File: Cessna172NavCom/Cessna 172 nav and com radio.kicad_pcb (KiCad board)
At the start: 2 copper layers, 180 x 38 mm, 52 parts, among them J1 Conn_02x12_Odd_Even, J2 Barrel_Jack_MountingPin, J3 Conn_01x05, SW1 SW_Push, SW2 SW_Push, SW3 SW_Push, SW4 Tuning encoder, SW5 Tuning encoder, SW6 Tuning encoder, U1 MAX7219 COM standby, U2 3651A, U3 MAX7219 COM standby, U4 3651A, U5 MAX7219 COM standby, U6 3651A, U7 MAX7219 COM standby, U8 3651A

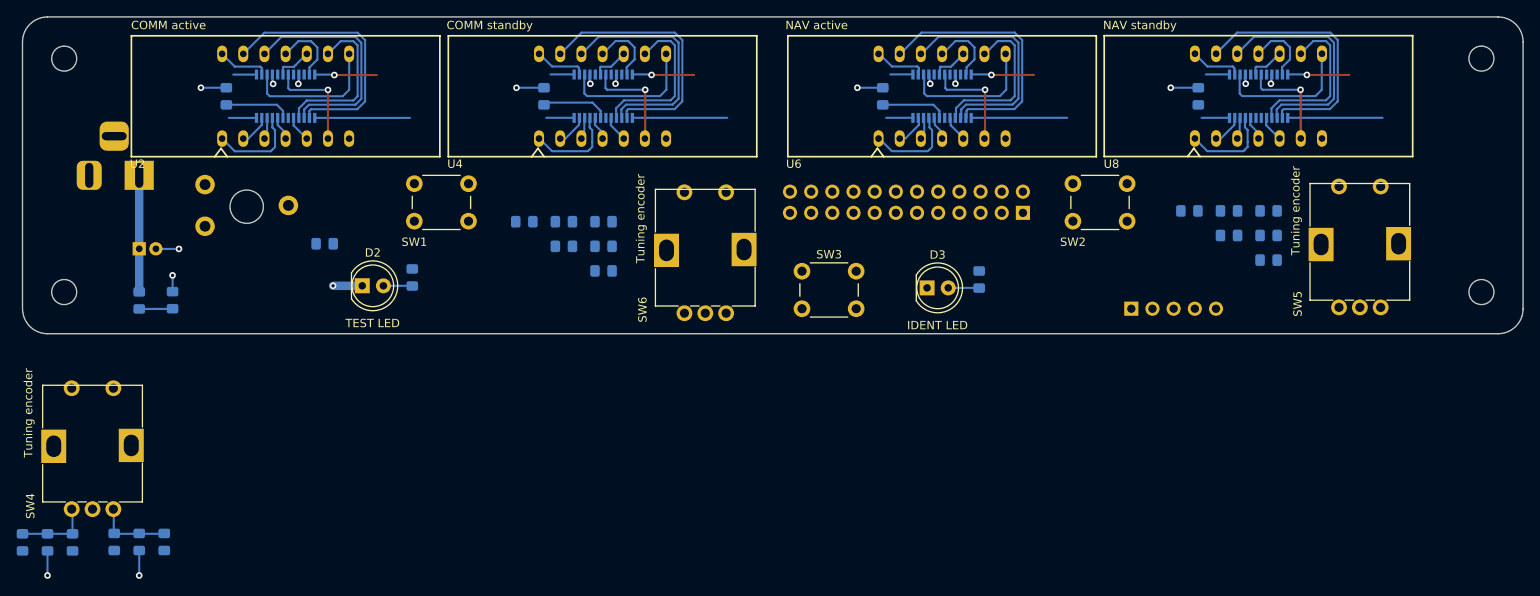
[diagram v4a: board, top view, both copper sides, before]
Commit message: Switch to USB for power, all parts on board
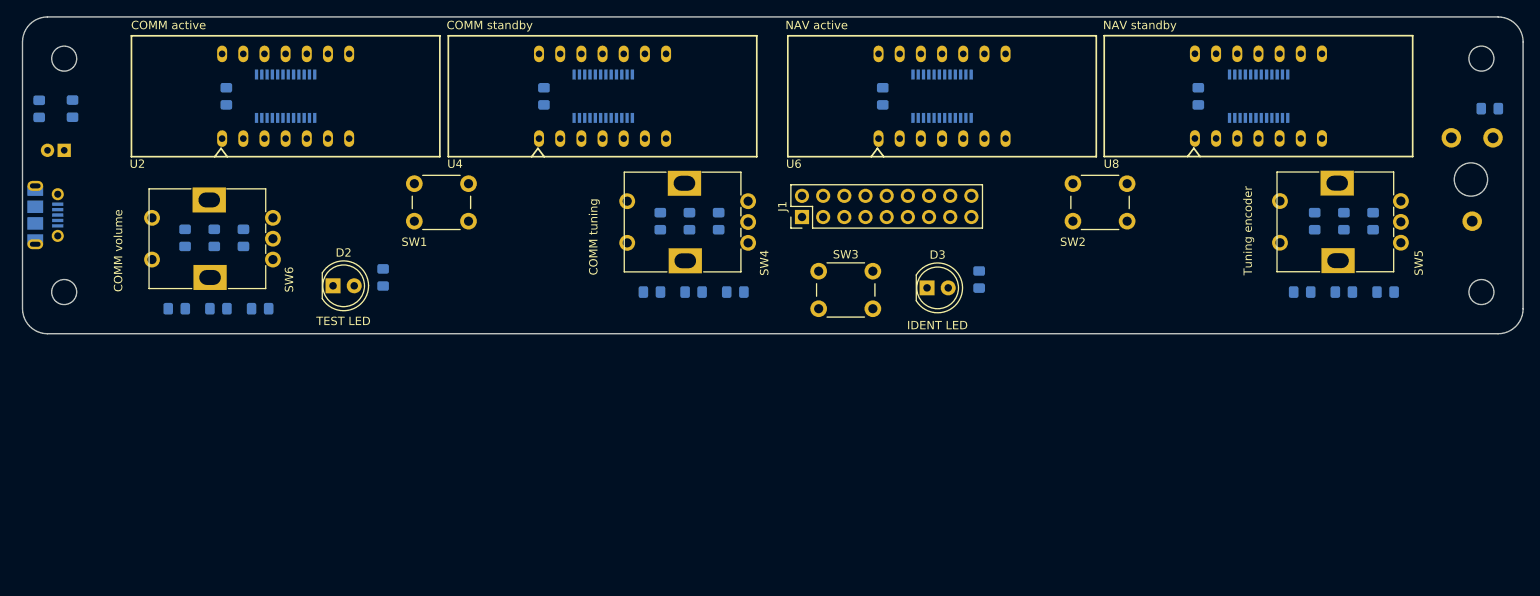
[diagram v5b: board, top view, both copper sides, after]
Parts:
- removed J3: Conn_01x05, Connector_PinHeader_2.54mm:PinHeader_1x05_P2.54mm_Vertical
- J1: value Conn_02x12_Odd_Even -> Conn_02x09_Odd_Even; footprint Connector_PinHeader_2.54mm:PinHeader_2x12_P2.54mm_Vertical -> Connector_PinHeader_2.54mm:PinHeader_2x09_P2.54mm_Vertical; moved to F.Cu
- J2: value Barrel_Jack_MountingPin -> USB_B_Micro; footprint Cessna 172 nav and com radio:BarrelJack_Horizontal -> Connector_USB:USB_Micro-B_Molex-105017-0001
- SW4: value Tuning encoder -> COMM tuning
- SW6: value Tuning encoder -> COMM volume
- moved RV1 154.6 mm to (206.4, 134.5), turned to 270 degrees
- moved R1 140.7 mm to (206.0, 131.0)
- moved R7 85.0 mm to (115.5, 153.0), turned to 180 degrees
- moved C6 83.1 mm to (110.5, 153.0), turned to 180 degrees
- moved R8 82.1 mm to (113.5, 144.5)
- moved R5 81.3 mm to (105.5, 153.0), turned to 0 degrees
- moved C7 76.4 mm to (110.0, 144.5)
- moved SW4 76.0 mm to (109.5, 144.5), turned to 90 degrees
- moved R6 70.9 mm to (106.5, 144.5)
- moved SW6 59.5 mm to (52.5, 146.5), turned to 90 degrees
- moved R14 50.2 mm to (49.5, 146.5), turned to 270 degrees
- moved C10 46.8 mm to (53.5, 155.0)
- moved R13 43.0 mm to (48.5, 155.0), turned to 0 degrees
- moved C11 42.0 mm to (53.0, 146.5), turned to 270 degrees
- moved R15 41.4 mm to (58.5, 155.0)
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- renumbered REF** to H1, REF** to H2, REF** to H3, REF** to H4
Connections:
- J1 pad 1: +5V -> GND
- J1 pad 11: NAV_TX_SW -> COMM_VOL_LEFT
- J1 pad 13: COMM_VOL_LEFT -> COMM_VOL_RIGHT
- J1 pad 15: COMM_VOL_RIGHT -> IDENT_SW
- J1 pad 17: IDENT_SW -> IDENT_LED
- J1 pad 3: GND -> NAV_LEFT
- J1 pad 5: NAV_LEFT -> NAV_RIGHT
- J1 pad 7: NAV_RIGHT -> NAV_KHZ_SW
- J1 pad 9: NAV_KHZ_SW -> NAV_TX_SW
- J2 pad 2: GND -> Net-(J2-Pad2)
- U7 pad 24: DOUT -> /sheet5F613961/DOUT
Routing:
- net CLK: track 45.7 -> 0.00 mm
- net +5V: track 37.4 -> 0.00 mm
- net GND: track 36.1 -> 0.00 mm, vias 17 -> 0
- net /sheet5F613961/SEG_A: track 31.4 -> 0.00 mm
- net /sheet5F611637/SEG_A: track 31.4 -> 0.00 mm
- net /5 digit LCD display/SEG_A: track 31.4 -> 0.00 mm
- net /sheet5F613960/SEG_A: track 31.4 -> 0.00 mm
- net LOAD: track 29.8 -> 0.00 mm, vias 4 -> 0
- net /sheet5F613961/SEG_F: track 27.9 -> 0.00 mm
- net /sheet5F613960/SEG_F: track 27.9 -> 0.00 mm
- net /sheet5F611637/SEG_F: track 27.9 -> 0.00 mm
- net /5 digit LCD display/SEG_F: track 27.9 -> 0.00 mm
- net /sheet5F613961/SEG_B: track 19.3 -> 0.00 mm
- net /sheet5F613960/SEG_B: track 19.3 -> 0.00 mm
- net /sheet5F611637/SEG_B: track 19.3 -> 0.00 mm
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
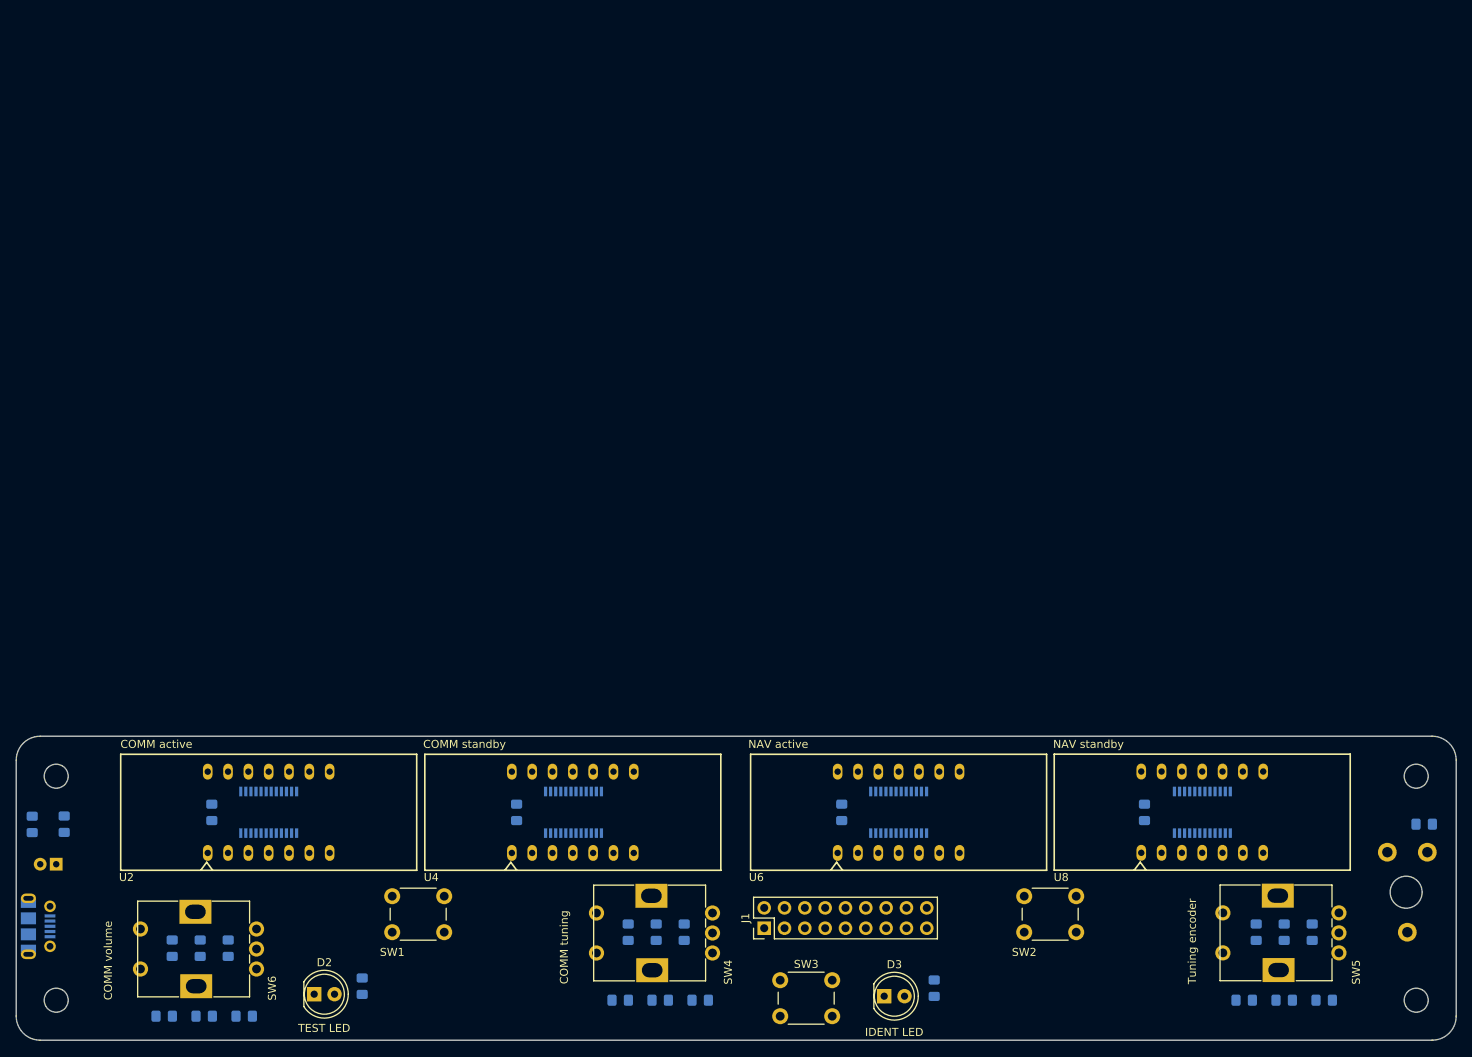
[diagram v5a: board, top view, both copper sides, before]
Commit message: Updated board size and parts placement
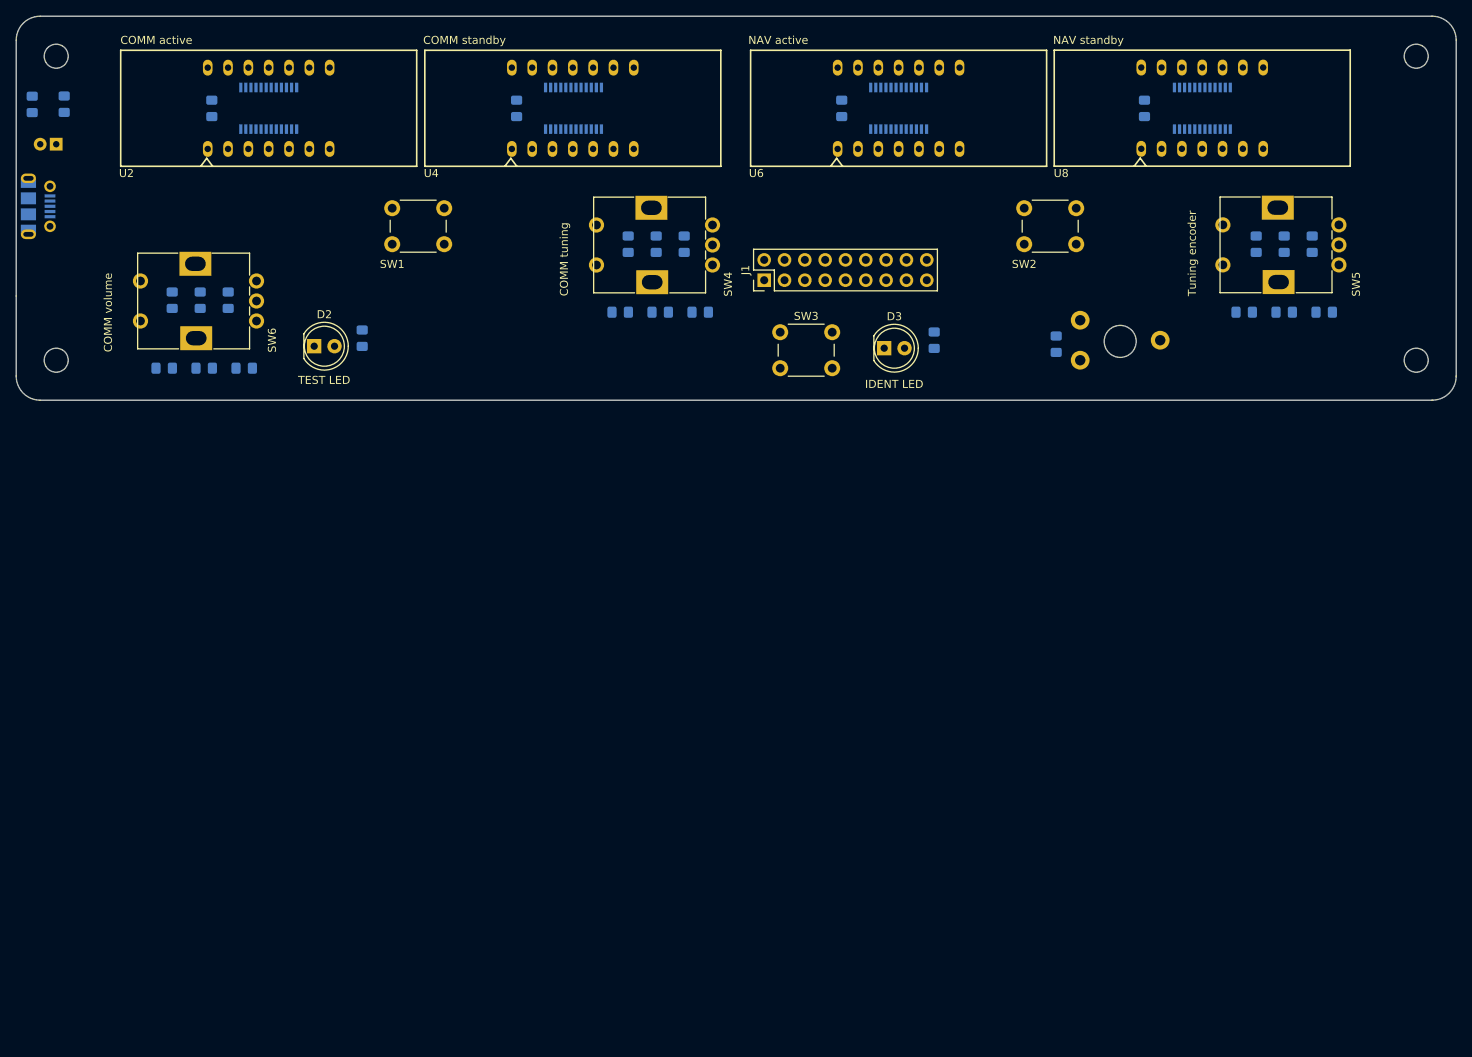
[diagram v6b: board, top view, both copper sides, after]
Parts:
- moved C1 90.0 mm to (35.0, 46.0)
- moved D1 90.0 mm to (32.0, 41.0)
- moved H1 90.0 mm to (35.0, 35.0)
- moved H3 90.0 mm to (205.0, 35.0)
- moved J2 90.0 mm to (32.8, 53.8)
- moved R2 90.0 mm to (36.0, 41.0)
- moved U1 88.0 mm to (61.6, 41.5)
- moved U2 88.0 mm to (61.6, 41.5)
- moved U3 88.0 mm to (99.7, 41.5)
- moved U4 88.0 mm to (99.6, 41.5)
- moved U5 88.0 mm to (140.3, 41.5)
- moved U6 88.0 mm to (140.3, 41.5)
- moved U7 88.0 mm to (178.3, 41.5)
- moved U8 88.0 mm to (178.3, 41.5)
- moved C2 88.0 mm to (54.5, 41.5)
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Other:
- board size 180 x 38 mm -> 180 x 48 mm

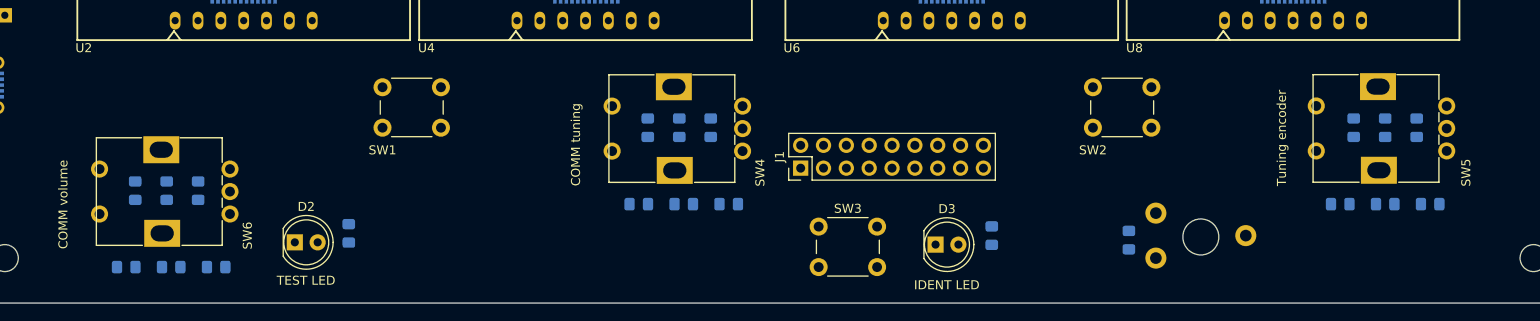
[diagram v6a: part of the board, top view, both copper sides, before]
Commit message: Updated rotary encoder with proper footprint
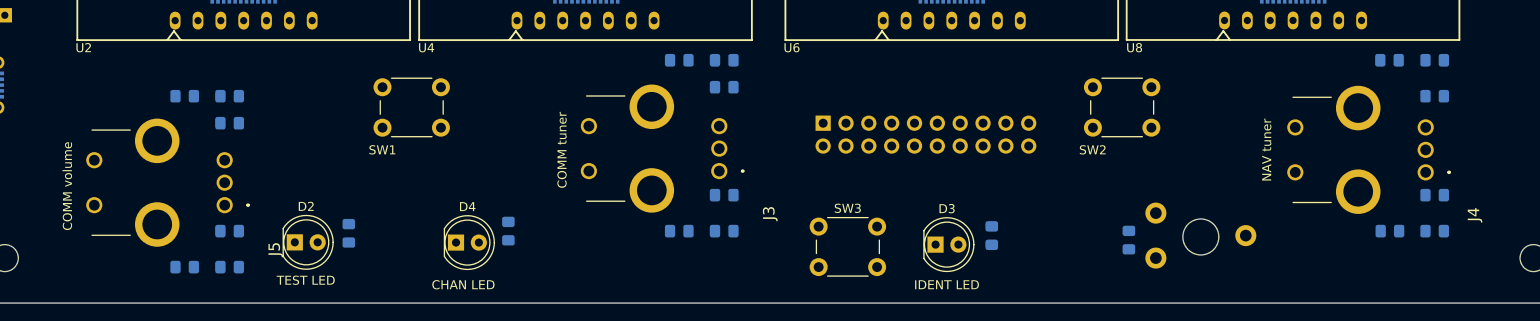
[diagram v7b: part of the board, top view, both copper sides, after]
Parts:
- removed SW4: COMM tuning, Cessna 172 nav and com radio:EN11-HSM1BF20
- removed SW5: Tuning encoder, Cessna 172 nav and com radio:EN11-HSM1BF20
- removed SW6: COMM volume, Cessna 172 nav and com radio:EN11-HSM1BF20
- added D4: LED, LED_THT:LED_D5.0mm, F.Cu at (85.2, 71.3)
- added J3: EN11-HSM1BF20, SamacSys_Parts:EN11HSM1BF20, F.Cu at (114.5, 63.3)
- added J4: EN11-HSM1BF20, SamacSys_Parts:EN11HSM1BF20, F.Cu at (193.0, 63.5)
- added J5: EN11-HSM1BF20, SamacSys_Parts:EN11HSM1BF20, F.Cu at (59.5, 67.1)
- added R17: 220k, Resistor_SMD:R_0805_2012Metric_Pad1.15x1.40mm_HandSolder, B.Cu at (91.0, 70.0)
- J1: value Conn_02x09_Odd_Even -> Conn_02x10_Odd_Even; footprint Connector_PinHeader_2.54mm:PinHeader_2x09_P2.54mm_Vertical -> Connector_PinHeader_2.54mm:PinHeader_2x10_P2.54mm_Vertical; moved to B.Cu
- moved C11 12.6 mm to (60.0, 55.0), turned to 0 degrees
- moved R14 11.9 mm to (55.0, 55.0), turned to 180 degrees
- moved C9 9.30 mm to (194.0, 51.0), turned to 0 degrees
- moved C7 9.01 mm to (115.0, 51.0), turned to 0 degrees
- moved R10 8.49 mm to (189.0, 51.0), turned to 0 degrees
- moved R16 8.28 mm to (60.0, 58.0), turned to 0 degrees
- moved R6 8.28 mm to (110.0, 51.0), turned to 0 degrees
- moved C10 6.50 mm to (60.0, 74.0)
- moved R13 6.50 mm to (55.0, 74.0)
- moved R9 6.29 mm to (189.0, 70.0)
- moved C8 6.26 mm to (194.0, 70.0)
- moved J1 5.59 mm to (126.0, 58.0), turned to 270 degrees
- moved C6 5.41 mm to (115.0, 70.0)
- moved R5 5.41 mm to (110.0, 70.0)
- moved R8 4.74 mm to (115.0, 54.0), turned to 0 degrees
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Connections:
- net /Tuning rotary encoder and switch/A renamed /Tuning rotary encoder and switch/A1
- net /Tuning rotary encoder and switch/B renamed /Tuning rotary encoder and switch/B1
- net /sheet5F5DD32A/A renamed /sheet5F5DD32A/A1
- net /sheet5F5DD32A/B renamed /sheet5F5DD32A/B1
- net /sheet5F5E0D6C/A renamed /sheet5F5E0D6C/A1
- net /sheet5F5E0D6C/B renamed /sheet5F5E0D6C/B1
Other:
- board text added: "CHAN LED"
- board text added: "COMM tuner"
- board text added: "COMM volume"
- board text added: "NAV tuner"

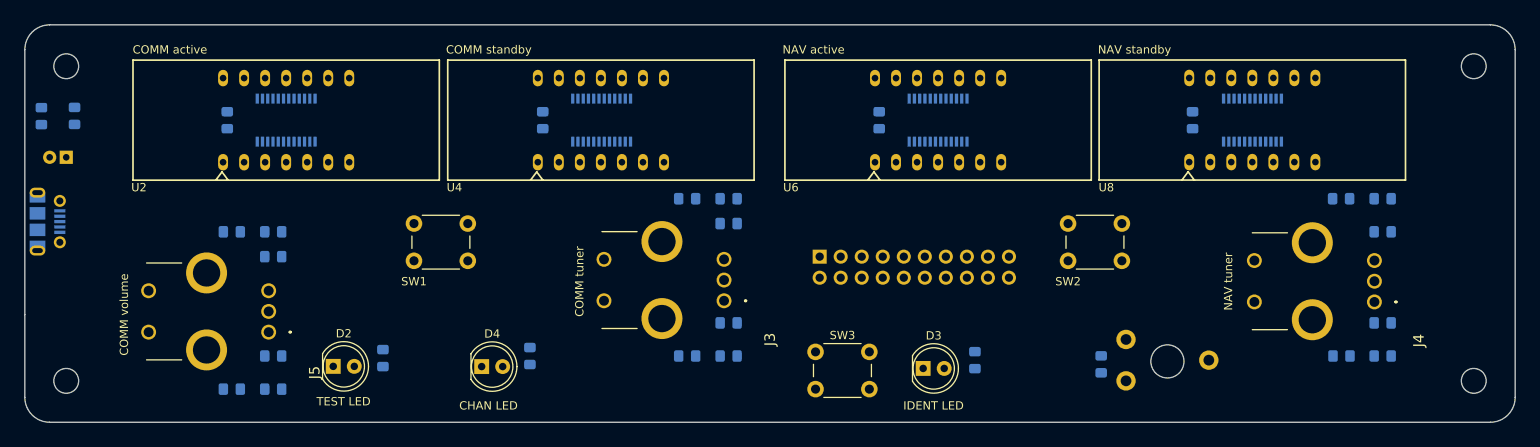
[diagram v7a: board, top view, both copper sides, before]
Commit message: Connection, footprint, and layout updates
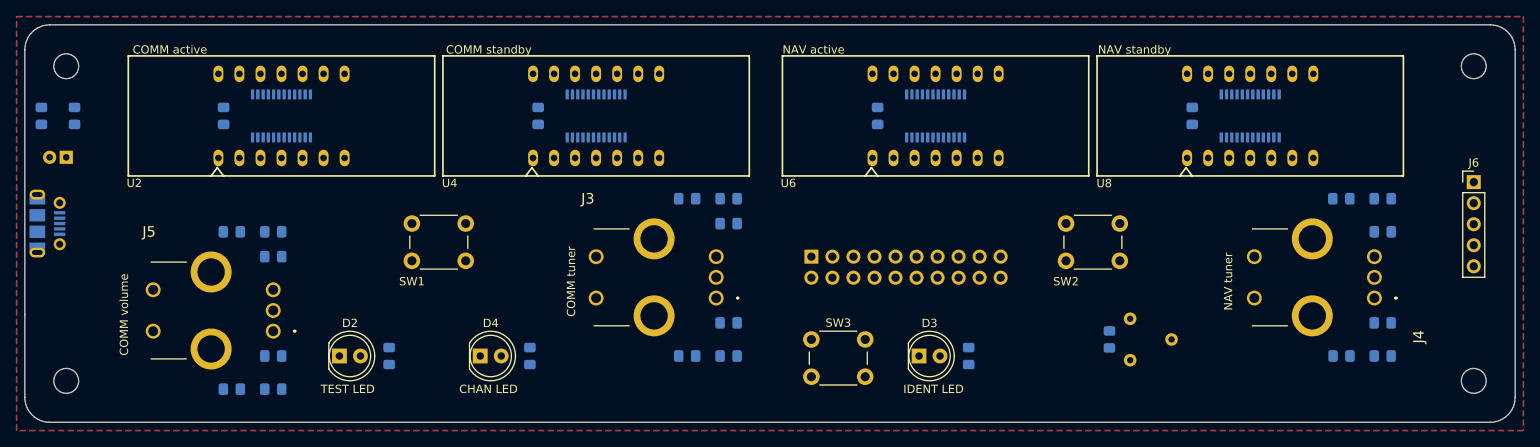
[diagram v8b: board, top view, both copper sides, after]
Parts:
- added J6: Conn_01x05, Connector_PinHeader_2.54mm:PinHeader_1x05_P2.54mm_Vertical, F.Cu at (205.0, 49.0)
- RV1: footprint Potentiometer_THT:Potentiometer_Piher_PT-10-V10_Vertical_Hole -> Cessna 172 nav and com radio:A-2506 trimpot resistor
- moved R1 3.16 mm to (161.0, 68.0)
- moved RV1 3.00 mm to (166.0, 68.0), turned to 90 degrees
- moved D3 1.58 mm to (138.0, 70.0)
- moved SW3 1.58 mm to (125.0, 68.0)
- moved D2 1.46 mm to (68.0, 70.0)
- moved D4 1.29 mm to (85.0, 70.0)
- moved J3 1.00 mm to (113.5, 63.0)
- moved J1 1.00 mm to (125.0, 58.0)
- moved R4 0.90 mm to (144.0, 70.0)
- moved U3 0.84 mm to (99.0, 41.0)
- moved R3 0.79 mm to (74.0, 70.0)
- moved U4 0.77 mm to (99.0, 41.0)
- moved U1 0.76 mm to (61.0, 41.0)
- moved U2 0.76 mm to (61.0, 41.0)
- moved C3 0.76 mm to (92.0, 41.0)
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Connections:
- J1 pad 1: GND -> LOAD
- J1 pad 10: COMM_RIGHT -> CHAN_LED
- J1 pad 11: COMM_VOL_LEFT -> COMM_KHZ_SW
- J1 pad 12: COMM_KHZ_SW -> IDENT_SW
- J1 pad 13: COMM_VOL_RIGHT -> GND
- J1 pad 14: COMM_TX_SW -> IDENT_LED
- J1 pad 15: IDENT_SW -> GND
- J1 pad 16: TEST_SW -> NAV_LEFT
- J1 pad 17: IDENT_LED -> COMM_TX_SW
- J1 pad 18: TEST_LED -> NAV_RIGHT
- J1 pad 19: Net-(J1-Pad19) -> NAV_TX_SW
- J1 pad 2: LOAD -> COMM_VOL_LEFT
- J1 pad 20: CHAN_LED -> NAV_KHZ_SW
- J1 pad 3: NAV_LEFT -> CLK
- J1 pad 4: CLK -> COMM_VOL_RIGHT
- J1 pad 5: NAV_RIGHT -> DIN
- J1 pad 6: DIN -> TEST_SW
- J1 pad 7: NAV_KHZ_SW -> COMM_LEFT
- J1 pad 8: COMM_LEFT -> TEST_LED
- J1 pad 9: NAV_TX_SW -> COMM_RIGHT
- U7 pad 24: /sheet5F613961/DOUT -> DOUT
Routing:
- added copper zone on B.Cu, net (none)
- added copper zone on F.Cu, net (none)
